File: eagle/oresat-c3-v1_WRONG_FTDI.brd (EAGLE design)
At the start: 99.8 x 94.7 mm, 168 parts, among them J1 J-SAMTEC-TFM-110-X1-XXX-D-RA, J10 U.FL, J11 U.FL, J13 U.FL, J14 U.FL, J15 HARWIN-2X8X1.27, J19 HARWIN-2X8X1.27, J2 U.FL, J3 U.FL, J4 U.FL, J6 J-SAMTEC-TFM-120-X1-XXX-D-RA, J7 FTSH-105-XX-X-DV-K, J8 U.FL, J9 U.FL, Q1 MOSFET-PCH-SOT23-6, U1 MAX892LEUA+T21-0036K-L, U11 U-ONSEMI-AX5043, U12 LP2985XX-N, U13 U-ONSEMI-AX5043, U14 LP2985XX-N, U2 TCAN330, U3 TCAN330, U4 TPS259621 - eFuse, U5 TPS62111RSA, U6 MAX6374KA-T21-0078H-L, U7 STM32F446RE, U9 SFEM016GB1EM1TO-A-HG-111-STD, X1 16MHZ-2.5x2mm, X3 TAITIEN-TY, X4 TAITIEN-TY

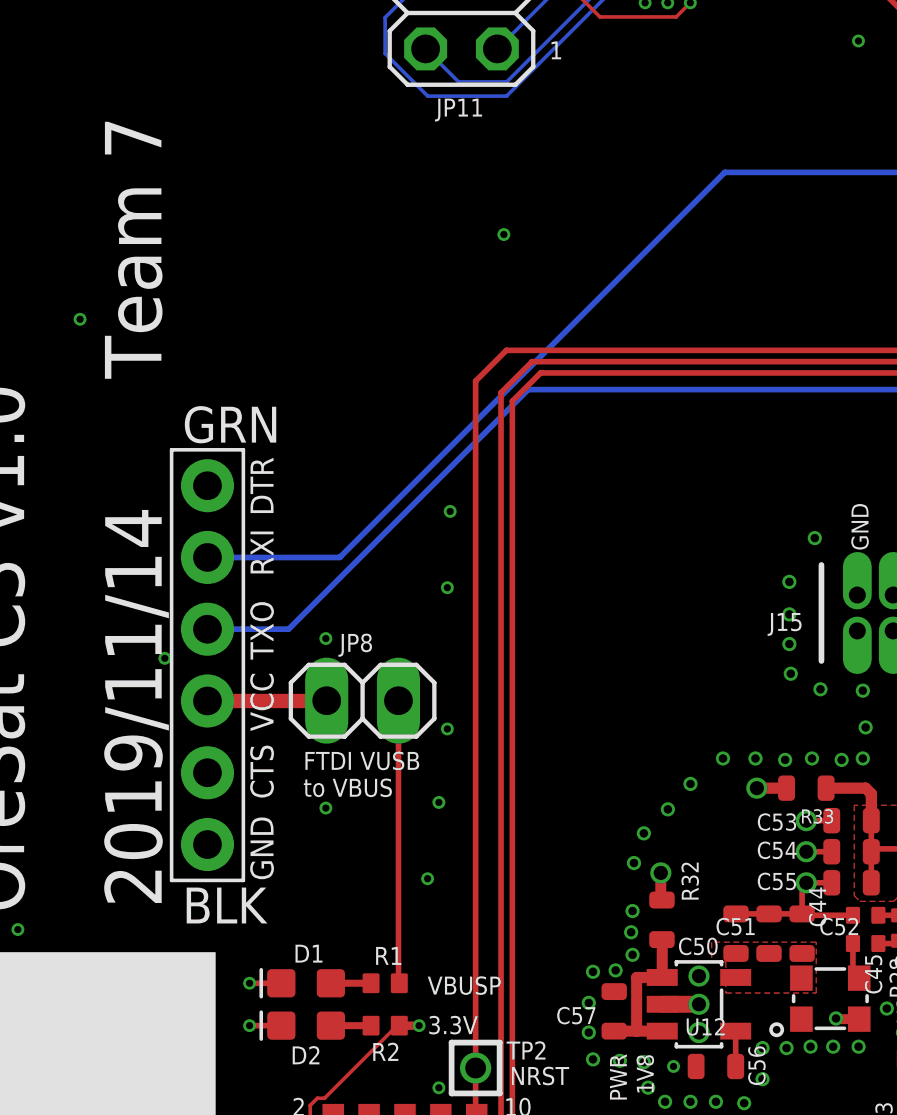
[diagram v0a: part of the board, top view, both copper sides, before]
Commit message: switched the TX and RX pins to be the correct way
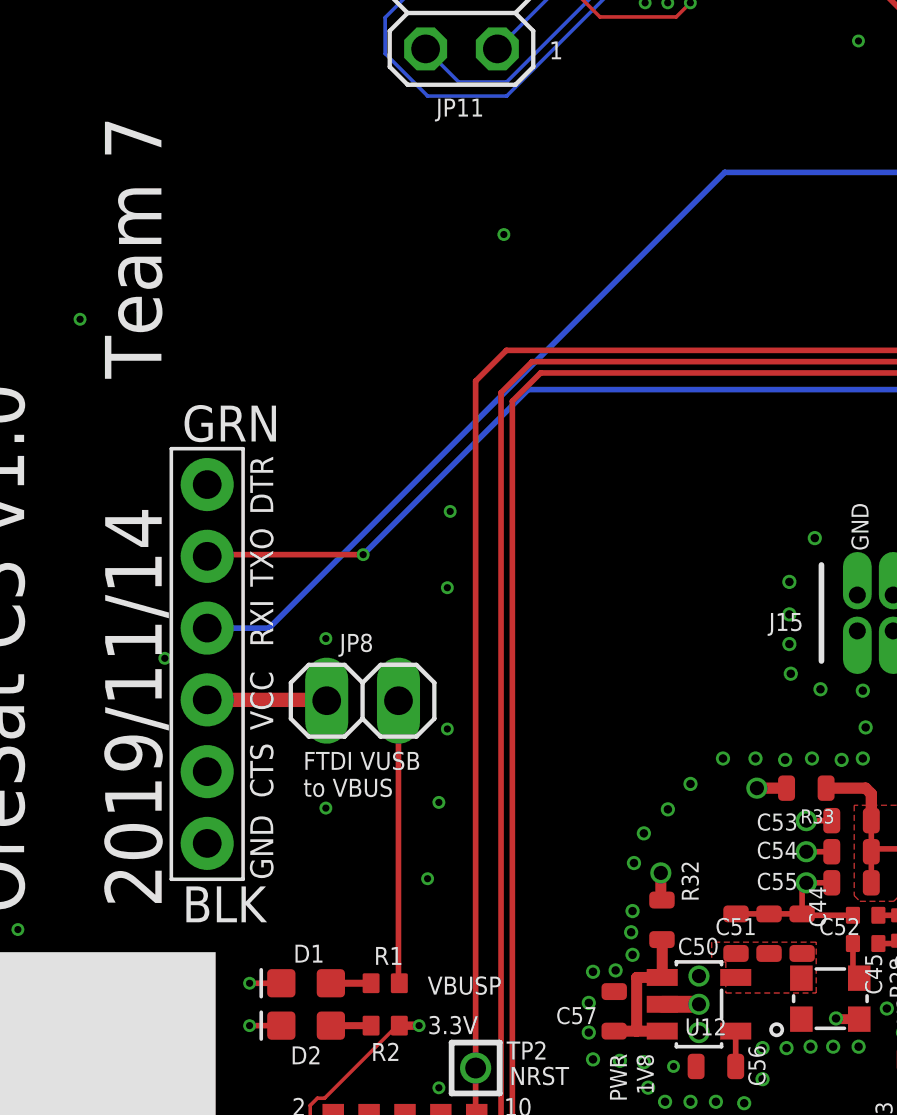
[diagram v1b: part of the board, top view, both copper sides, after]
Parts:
- removed U$2: C3_FTDI_CONN, TrueC3_FTDIlbr:6_PIN_SERIAL_TARGET_SIDE_W_SILK
- added J5: (no value), SparkFun-Connectors:6_PIN_SERIAL_TARGET_SIDE_W_SILK
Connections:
- net GND: now also J5.P$6; no longer U$2.P$6
- net N$406: now also J5.P$4; no longer U$2.P$4
- net USART2_RX: now also J5.P$2; no longer U$2.P$3
- net USART2_TX: now also J5.P$3; no longer U$2.P$2
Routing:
- net USART2_RX: track 43.9 -> 42.8 mm, vias 1 -> 2
- net USART2_TX: track 41.9 -> 43.0 mm
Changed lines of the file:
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@@
 <attribute name="VALUE" x="86.44" y="80.93" size="0.6096" layer="27" font="vector" ratio="20" rot="R90" align="top-left"/>
 </element>
+<element name="J5" library="SparkFun-Connectors" library_urn="urn:adsk.eagle:library:513" package="6_PIN_SERIAL_TARGET_SIDE_W_SILK" package3d_urn="urn:adsk.eagle:package:37995/1" value="" x="13.5" y="26.8" smashed="yes" rot="R270"/>
 <element name="H1" library="SparkFun-Hardware" library_urn="urn:adsk.eagle:library:519" package="STAND-OFF-TIGHT" package3d_urn="urn:adsk.eagle:package:38629/1" value="STAND-OFFTIGHT" x="93" y="6" locked="yes" smashed="yes">
 <attribute name="VALUE" x="93" y="4.349" size="0.6096" layer="27" font="vector" ratio="20" align="top-center"/>
@@
 <attribute name="NAME" x="70.8" y="16.7" size="0.8" layer="25" font="vector" ratio="20"/>
 </element>
-<element name="U$2" library="TrueC3_FTDIlbr" package="6_PIN_SERIAL_TARGET_SIDE_W_SILK" value="C3_FTDI_CONN" x="13.51" y="26.76" smashed="yes" rot="R270"/>
 </elements>
 <signals>
@@
 <contactref element="J2" pad="1"/>
 <contactref element="J2" pad="2"/>
+<contactref element="J5" pad="P$6"/>
 <via x="10" y="4.5" extent="1-16" drill="0.254"/>
 <contactref element="J7" pad="9"/>
@@
 <wire x1="38.905" y1="19.255" x2="40.11" y2="19.255" width="0.3" layer="1"/>
 <wire x1="40.11" y1="19.255" x2="40.11" y2="19.29" width="0.3" layer="1"/>
-<contactref element="U$2" pad="P$6"/>
 </signal>
 <signal name="SPI1_SCK">
@@
 <wire x1="48.385" y1="46.785" x2="48.385" y2="47.125" width="0.2" layer="1"/>
 <via x="45.8" y="44.2" extent="1-16" drill="0.254"/>
-<wire x1="31.82" y1="44.2" x2="18.23" y2="30.61" width="0.2" layer="16"/>
-<contactref element="U$2" pad="P$2"/>
-<wire x1="13.51" y1="30.57" x2="18.19" y2="30.57" width="0.2" layer="16"/>
-<wire x1="18.19" y1="30.57" x2="18.23" y2="30.61" width="0.2" layer="16"/>
+<contactref element="J5" pad="P$3"/>
+<wire x1="13.5" y1="28.07" x2="15.69" y2="28.07" width="0.2" layer="16"/>
+<wire x1="31.82" y1="44.2" x2="15.69" y2="28.07" width="0.2" layer="16"/>
 </signal>
 <signal name="USART2_RX">
 <wire x1="50.235" y1="45.275" x2="49.825" y2="45.275" width="0.2" layer="1"/>
 <wire x1="49.825" y1="45.275" x2="41.0606" y2="36.5106" width="0.2" layer="1"/>
+<wire x1="24.8606" y1="36.5106" x2="19.02" y2="30.67" width="0.2" layer="16"/>
 <contactref element="U7" pad="17"/>
 <wire x1="41.0606" y1="36.5106" x2="24.8606" y2="36.5106" width="0.2" layer="16"/>
 <via x="41.0606" y="36.5106" extent="1-16" drill="0.254"/>
-<contactref element="U$2" pad="P$3"/>
-<wire x1="16.38" y1="28.03" x2="13.51" y2="28.03" width="0.2" layer="16"/>
-<wire x1="24.8606" y1="36.5106" x2="16.38" y2="28.03" width="0.2" layer="16"/>
+<contactref element="J5" pad="P$2"/>
+<via x="19.02" y="30.67" extent="1-16" drill="0.254"/>
+<wire x1="19.02" y1="30.67" x2="13.56" y2="30.67" width="0.2" layer="1"/>
+<wire x1="13.56" y1="30.67" x2="13.5" y2="30.61" width="0.2" layer="1"/>
 </signal>
 <signal name="BOOT0">
@@
 </signal>
 <signal name="N$406">
+<contactref element="J5" pad="P$4"/>
 <contactref element="JP8" pad="2"/>
-<contactref element="U$2" pad="P$4"/>
-<wire x1="13.51" y1="25.49" x2="17.72" y2="25.49" width="0.508" layer="1"/>
-<wire x1="17.72" y1="25.49" x2="17.73" y2="25.5" width="0.508" layer="1"/>
+<wire x1="13.5" y1="25.53" x2="17.7" y2="25.53" width="0.508" layer="1"/>
+<wire x1="17.7" y1="25.53" x2="17.73" y2="25.5" width="0.508" layer="1"/>
 </signal>
 <signal name="AUX-1">
